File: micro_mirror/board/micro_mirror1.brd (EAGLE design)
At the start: 128.3 x 76.2 mm, 163 parts, among them IC1 74LV7014, IC2 74LV02, IC3 74LV08, IC4 LM324D, IC5 LM324D, J1 POWER_JACKPTH_LOCK, U8 TPS62160

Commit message: in progress, changing copper spacing
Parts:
- C1: value 10nF-L -> 10nF-H
- R3: value 1M -> 10M
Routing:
- net HV_ADJ: track 72.0 -> 69.3 mm

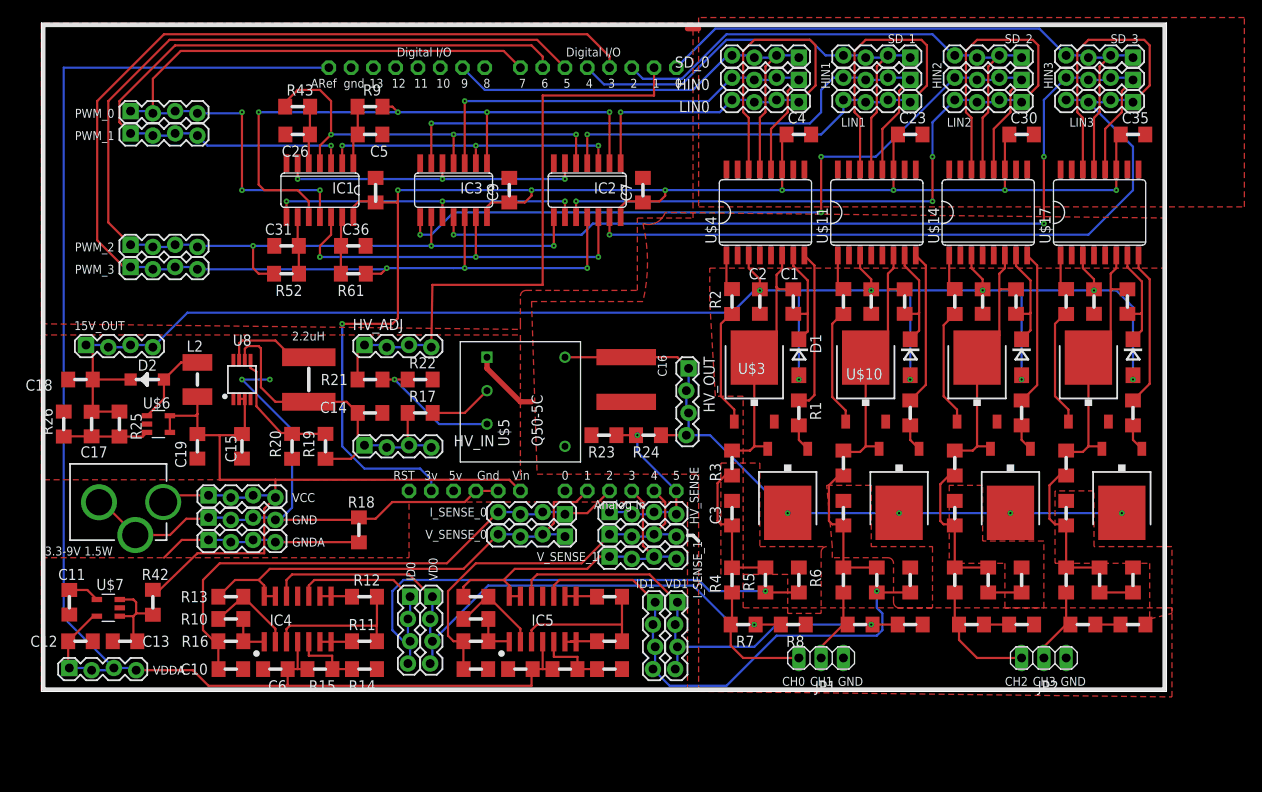
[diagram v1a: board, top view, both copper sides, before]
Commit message: bigger gap for output connectors
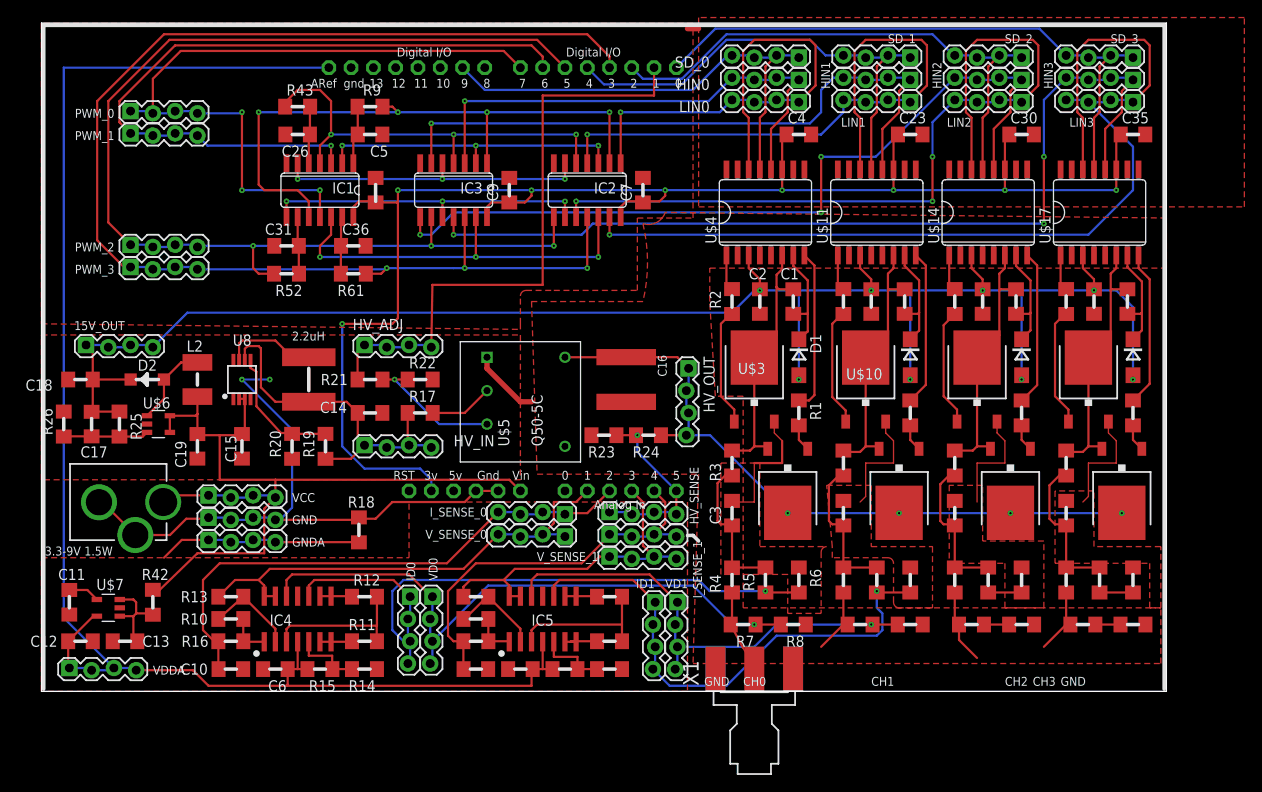
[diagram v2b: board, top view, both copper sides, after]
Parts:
- removed JP1, JP2: (no value), pinhead:1X03
- added X1: SMA-142-0701-801/806, con-coax:J502-ND-142-0701-801/806
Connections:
- net GND: now also X1.G@1, X1.G@2, X1.G@3, X1.G@4; no longer JP1.3, JP2.3
- net VO0: now also X1.1; no longer JP1.1
- net VO1: no longer JP1.2
- net VO2: no longer JP2.1
- net VO3: no longer JP2.2
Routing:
- net GND: track 81.5 -> 135.5 mm
- net VO2: track 13.6 -> 8.52 mm
- net VO0: track 14.5 -> 9.45 mm
- net VO3: track 9.20 -> 7.93 mm
- net VO1: track 9.20 -> 7.93 mm

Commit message: making gap > 40 mil to handle 1kV.
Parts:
- added X2, X3, X4: SMA-142-0701-801/806, con-coax:J502-ND-142-0701-801/806
- moved C2 0.90 mm to (81.3, 45.1)
- moved C33 0.90 mm to (119.4, 45.1)
- moved R45 0.90 mm to (103.5, 45.1)
- moved R54 0.90 mm to (116.2, 45.1)
- moved C21 0.90 mm to (94.0, 45.1)
- moved C28 0.90 mm to (106.7, 45.1)
- moved R2 0.90 mm to (78.1, 45.1)
- moved R28 0.90 mm to (90.8, 45.1)
- moved R8 0.64 mm to (86.4, 7.62)
- moved X1 0.64 mm to (81.9, 0.00)
- moved R7 0.63 mm to (80.6, 7.62)
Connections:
- net GND: now also X2.G@1, X2.G@2, X2.G@3, X2.G@4, X3.G@1, X3.G@2, X3.G@3, X3.G@4, X4.G@1, X4.G@2, X4.G@3, X4.G@4
- net VO1: now also X2.1
- net VO2: now also X3.1
- net VO3: now also X4.1
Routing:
- net GND: track 135.5 -> 400.4 mm, vias 2 -> 6
- net VO2: track 8.52 -> 14.2 mm
- net VD0: track 71.9 -> 76.5 mm
- net VO1: track 7.93 -> 11.4 mm
- net VO3: track 7.93 -> 10.8 mm
- net N$50: track 13.5 -> 16.1 mm
- net ID1: track 60.3 -> 62.5 mm
- net ID0: track 76.3 -> 78.2 mm
- net N$41: track 13.4 -> 15.3 mm
- net N$25: track 13.5 -> 15.0 mm
- net +15V: track 197.6 -> 198.8 mm
- net N$26: track 30.1 -> 31.2 mm
- net N$42: track 29.4 -> 30.5 mm
- net N$53: track 4.10 -> 3.20 mm
- net N$44: track 4.10 -> 3.20 mm
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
